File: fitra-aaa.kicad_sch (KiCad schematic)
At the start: 23 parts, among them J1 SM03B-SRSS-TB, M1 *, U2 LSM6DSV, U3 NPM2100-QEAA-R7

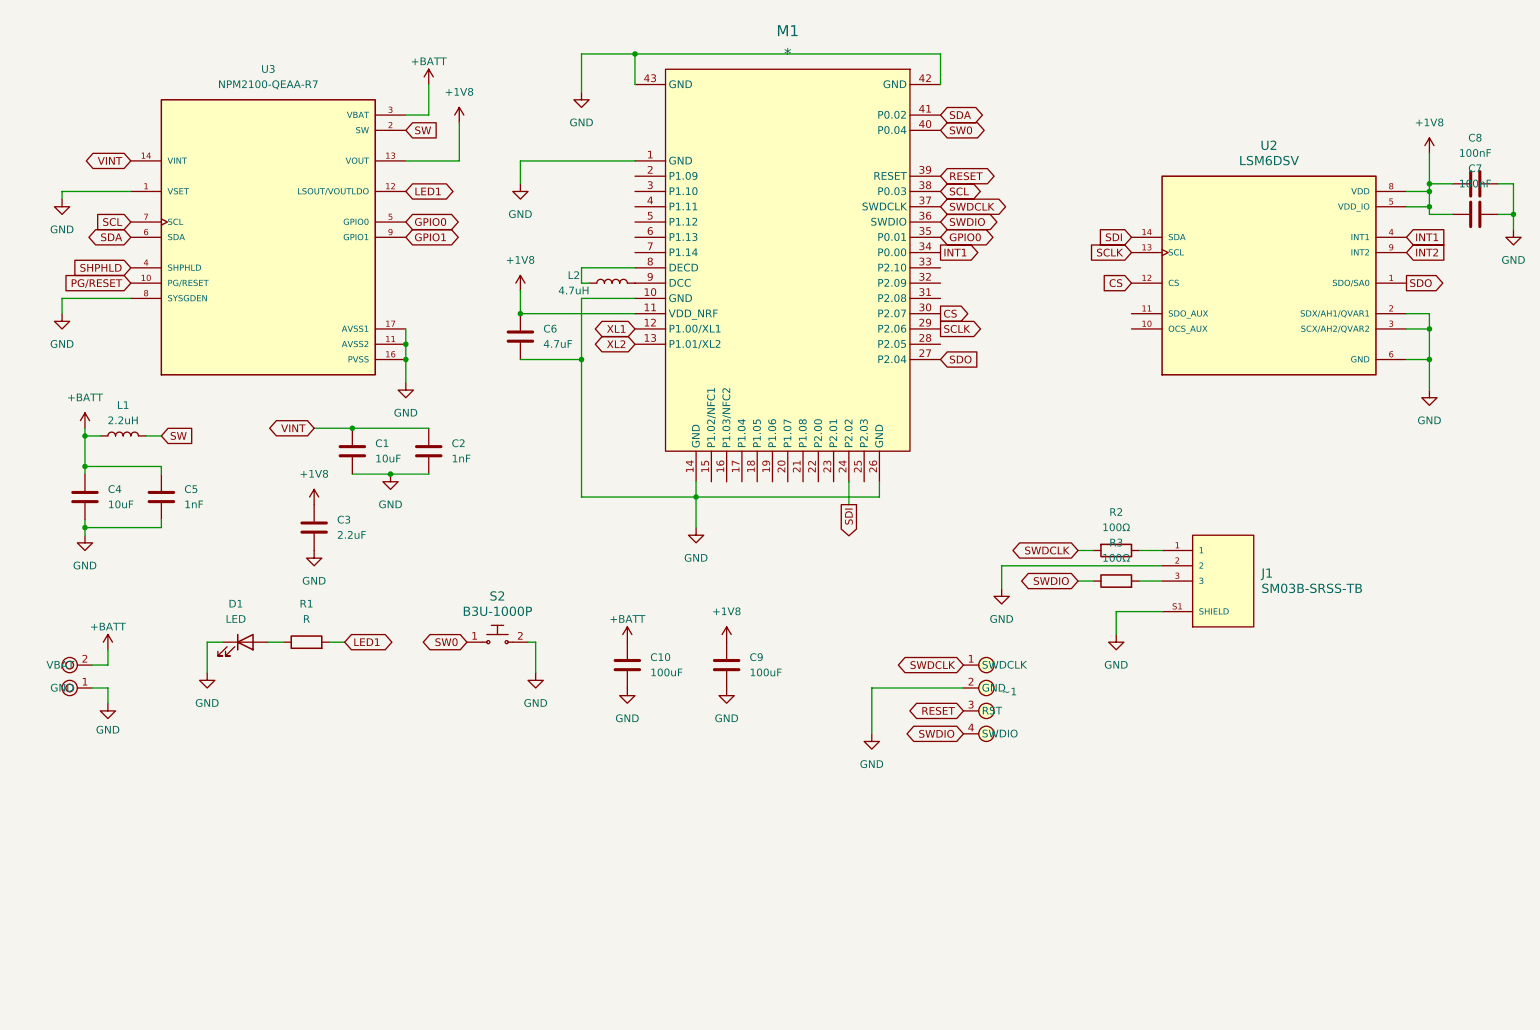
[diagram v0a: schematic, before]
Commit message: Update board for AN54LV module
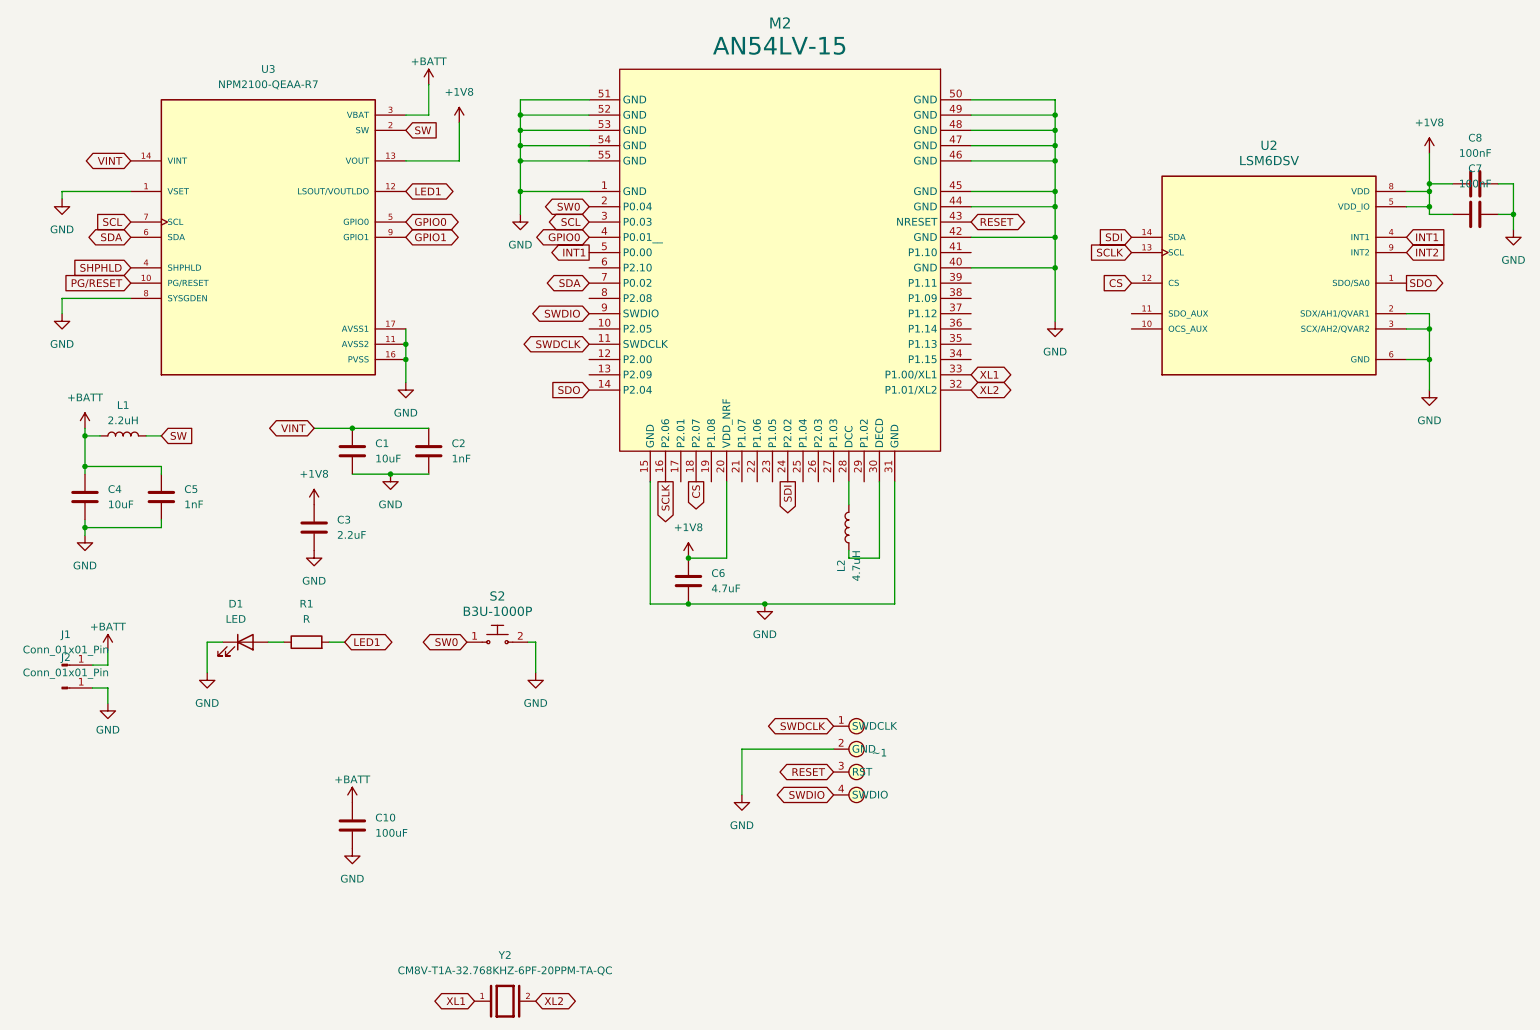
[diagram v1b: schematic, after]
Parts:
- removed BAT_thru2: (no value), local_lib:VBAT_thru, symbol local_lib:BAT_thru
- removed C9: 100uF, Capacitor_SMD:C_0805_2012Metric, symbol Device:C
- removed J1: SM03B-SRSS-TB, sm03b_lib:JST_SM03B-SRSS-TB_LF__SN_, symbol sm03b_lib:SM03B-SRSS-TB_LF__SN_
- removed M1: *, AN54LQ-15, symbol AN54LQ-15_SCHLIB_250212:AN54LQ-15
- removed R2, R3: 100Ω, Resistor_SMD:R_0201_0603Metric, symbol Device:R
- added J1, J2: Conn_01x01_Pin, Connector_Pin:Pin_D0.7mm_L6.5mm_W1.8mm_FlatFork, symbol Connector:Conn_01x01_Pin
- added M2: AN54LV-15, AN54LV-15-250919:AN54LV-15, symbol AN54LV-15-250919:AN54LV-15
- added Y2: CM8V-T1A-32.768KHZ-6PF-20PPM-TA-QC, se_CM8V-T1A-32.768KHZ-6PF-20PPM-TA-QC:XTAL_CM8V-T1A-32.768KHZ-6PF-20PPM-TA-QC, symbol CM8V-T1A-32.768KHZ-6PF-20PPM-TA-QC:CM8V-T1A-32.768KHZ-6PF-20PPM-TA-QC
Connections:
- net +1V8: now also M2.20 (VDD_NRF)
- net +BATT: now also J1.1 (Pin_1)
- net CS: now also M2.18 (P2.07)
- net GND: now also J2.1 (Pin_1), M2.1 (GND), M2.15 (GND), M2.31 (GND), M2.40 (GND), M2.42 (GND), M2.44 (GND), M2.45 (GND), M2.46 (GND), M2.47 (GND), M2.48 (GND), M2.49 (GND), M2.50 (GND), M2.51 (GND), M2.52 (GND), M2.53 (GND), M2.54 (GND), M2.55 (GND)
- net GPIO0: now also M2.4 (P0.01__)
- net INT1: now also M2.5 (P0.00)
- net RESET: now also M2.43 (NRESET)
- net SCL: now also M2.3 (P0.03)
- net SCLK: now also M2.16 (P2.06)
- net SDA: now also M2.7 (P0.02)
- net SDI: now also M2.24 (P2.02)
- net SDO: now also M2.14 (P2.04)
- net SW0: now also M2.2 (P0.04)
- net SWDCLK: now also M2.11 (SWDCLK)
- net SWDIO: now also M2.9 (SWDIO)
- net XL1: now also M2.33 (P1.00/XL1), Y2.1
- net XL2: now also M2.32 (P1.01/XL2), Y2.2
- net at L2.1: now also M2.30 (DECD)
- net at L2.2: now also M2.28 (DCC)
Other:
- moved on the sheet: C10, C6, L2, ~1
